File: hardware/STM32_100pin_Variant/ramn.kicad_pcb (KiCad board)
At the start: 2 copper layers, 93.6 x 70 mm, 139 parts, among them J1 USB_C_Micro, J2 Screw_Terminal_01x03, J3 , J4 , J5 , J6 , U1 STM32L4S7VITx, U10 STM32L4S7VITx, U11 ATA6561-GAQW-N, U12 NCV8163, U2 ATA6561-GAQW-N, U3 NCV8163, U4 STM32L4S7VITx, U5 ATA6561-GAQW-N, U6 NCV8163, U7 STM32L4S7VITx, U8 ATA6561-GAQW-N, U9 NCV8163, Y1 Crystal_GND24, Y2 Crystal_GND24, Y3 Crystal_GND24, Y4 Crystal_GND24

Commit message: Schematic wiring fix, added part numbers
- Fixed missing connections between VREF+ and VDDA, VREF- and VSSA on all ECUs

- Added component part numbers for crystal and CAN trx to schematic
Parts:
- renumbered C18 to C19, C19 to C20, C20 to C21, C21 to C22, C22 to C23, C23 to C24, C24 to C25, C25 to C26, C26 to C27, C27 to C28, C28 to C29, C29 to C30, C30 to C31, C31 to C32, C32 to C33, C33 to C34, C34 to C35, C35 to C36, C36 to C37, C37 to C38, C38 to C39, C39 to C40, C40 to C41, C41 to C42, C42 to C43, C43 to C44, C44 to C45, C45 to C46, C46 to C47, C47 to C48, C48 to C49, C49 to C50, C50 to C51, C51 to C52, C52 to C53, C53 to C54, C54 to C55, C55 to C56, C56 to C57, C57 to C58, C58 to C59, C59 to C60, C60 to C61, C61 to C62, C62 to C63, C63 to C64, C64 to C65, C65 to C66, C66 to C67, C67 to C68, C68 to C69, TP9 to TP8, TP10 to TP9
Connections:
- H1 pad : GND -> (no net)
- H2 pad : GND -> (no net)
- H3 pad : GND -> (no net)
- H4 pad : GND -> (no net)
- U1 pad 20: unconnected-(U1-Pad20) -> GND
- U1 pad 21: unconnected-(U1-Pad21) -> /usb_uc/3V3_ECU
- U10 pad 20: unconnected-(U10-Pad20) -> GND
- U10 pad 21: unconnected-(U10-Pad21) -> /ECUD/3V3_ECU
- U4 pad 20: unconnected-(U4-Pad20) -> GND
- U4 pad 21: unconnected-(U4-Pad21) -> /ECUB/3V3_ECU
- U7 pad 20: unconnected-(U7-Pad20) -> GND
- U7 pad 21: unconnected-(U7-Pad21) -> /ECUC/3V3_ECU
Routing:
- net GND: track 776.1 -> 772.8 mm
- net /usb_uc/3V3_ECU: track 114.8 -> 116.9 mm
- net /ECUB/3V3_ECU: track 109.4 -> 111.2 mm
- net /ECUC/3V3_ECU: track 116.1 -> 117.8 mm
- net /ECUD/3V3_ECU: track 129.1 -> 130.7 mm

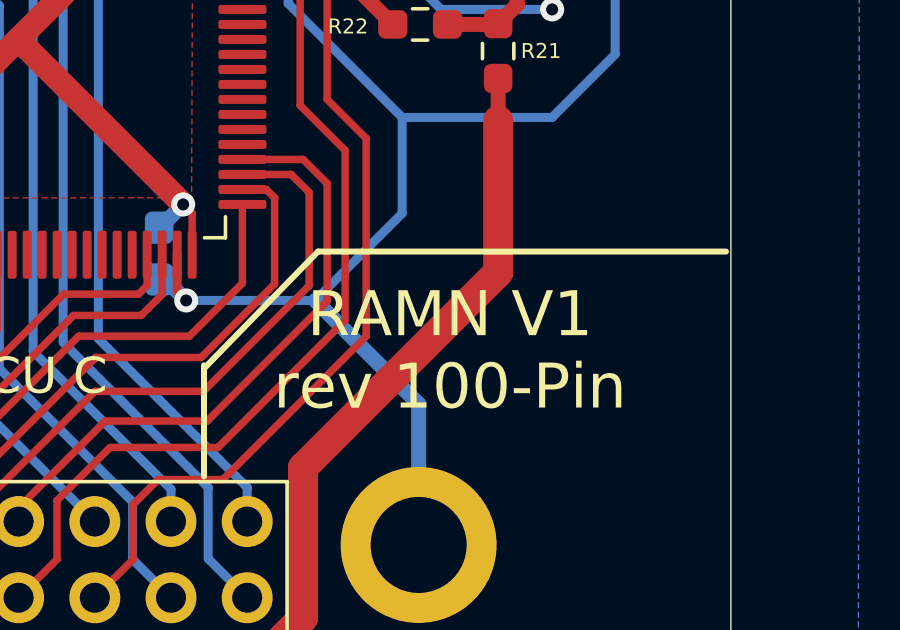
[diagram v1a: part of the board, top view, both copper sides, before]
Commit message: Electrical Fix
- Fixed missing VREF+/- connections on ECUs

- Updated version number to V1.1

- Updated Gerbers

- Updated schematic PDF
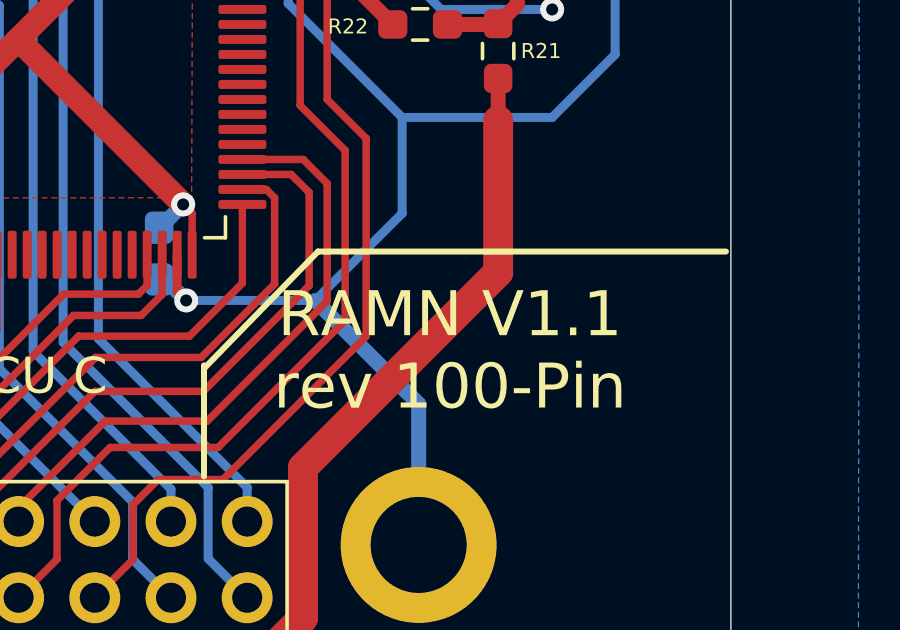
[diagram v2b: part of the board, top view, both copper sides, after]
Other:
- board text added: "RAMN V1.1 rev 100-Pin"
- board text removed: "RAMN V1 rev 100-Pin"
